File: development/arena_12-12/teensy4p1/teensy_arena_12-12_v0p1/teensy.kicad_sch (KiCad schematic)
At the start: 41 parts, among them J2 Conn_01x04, J3 Conn_01x04, U1 Teensy4.1, U2 74LVC2G17

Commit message: Finished preliminary layout for new 12-12 teensy 4.1 arena.
Includes source termination resistors and schmitt trigger buffers.
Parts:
- C1: footprint Capacitor_SMD:C_0603_1608Metric -> Capacitor_SMD:C_0402_1005Metric
- R10, R11, R12, R13, R14, R15, R16, R17, R18, R19, R20, R21, R22, R23, R24, R25, R26, R27, R28, R29, R3, R30, R31, R32, R33, R34, R35, R36, R37, R38, R4, R5, R6, R7, R8, R9: footprint Resistor_SMD:R_0603_1608Metric -> Resistor_SMD:R_0402_1005Metric
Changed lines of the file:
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@@
 			)
 		)
-		(property "Footprint" "Resistor_SMD:R_0603_1608Metric"
+		(property "Footprint" "Resistor_SMD:R_0402_1005Metric"
 			(at 255.27 147.828 90)
 			(effects
@@
 			)
 		)
-		(property "Footprint" "Resistor_SMD:R_0603_1608Metric"
+		(property "Footprint" "Resistor_SMD:R_0402_1005Metric"
 			(at 255.27 183.388 90)
 			(effects
@@
 			)
 		)
-		(property "Footprint" "Resistor_SMD:R_0603_1608Metric"
+		(property "Footprint" "Resistor_SMD:R_0402_1005Metric"
 			(at 255.27 112.268 90)
 			(effects
@@
 			)
 		)
-		(property "Footprint" "Resistor_SMD:R_0603_1608Metric"
+		(property "Footprint" "Resistor_SMD:R_0402_1005Metric"
 			(at 255.27 42.418 90)
 			(effects
@@
 			)
 		)
-		(property "Footprint" "Resistor_SMD:R_0603_1608Metric"
+		(property "Footprint" "Resistor_SMD:R_0402_1005Metric"
 			(at 255.27 61.468 90)
 			(effects
@@
 			)
 		)
-		(property "Footprint" "Resistor_SMD:R_0603_1608Metric"
+		(property "Footprint" "Resistor_SMD:R_0402_1005Metric"
 			(at 255.27 218.948 90)
 			(effects
@@
 			)
 		)
-		(property "Footprint" "Resistor_SMD:R_0603_1608Metric"
+		(property "Footprint" "Resistor_SMD:R_0402_1005Metric"
 			(at 255.27 122.428 90)
 			(effects
@@
 			)
 		)
-		(property "Footprint" "Resistor_SMD:R_0603_1608Metric"
+		(property "Footprint" "Resistor_SMD:R_0402_1005Metric"
 			(at 255.27 28.448 90)
 			(effects
@@
 			)
 		)
-		(property "Footprint" "Resistor_SMD:R_0603_1608Metric"
+		(property "Footprint" "Resistor_SMD:R_0402_1005Metric"
 			(at 255.27 132.588 90)
 			(effects
@@
 			)
 		)
-		(property "Footprint" "Resistor_SMD:R_0603_1608Metric"
+		(property "Footprint" "Resistor_SMD:R_0402_1005Metric"
 			(at 255.27 168.148 90)
 			(effects
@@
 			)
 		)
-		(property "Footprint" "Resistor_SMD:R_0603_1608Metric"
+		(property "Footprint" "Resistor_SMD:R_0402_1005Metric"
 			(at 255.27 33.528 90)
 			(effects
@@
 			)
 		)
-		(property "Footprint" "Resistor_SMD:R_0603_1608Metric"
+		(property "Footprint" "Resistor_SMD:R_0402_1005Metric"
 			(at 255.27 157.988 90)
 			(effects
@@
 			)
 		)
-		(property "Footprint" "Capacitor_SMD:C_0603_1608Metric"
+		(property "Footprint" "Capacitor_SMD:C_0402_1005Metric"
 			(at 155.9052 199.39 0)
 			(effects
@@
 			)
 		)
-		(property "Footprint" "Resistor_SMD:R_0603_1608Metric"
+		(property "Footprint" "Resistor_SMD:R_0402_1005Metric"
 			(at 255.27 76.708 90)
 			(effects
@@
 			)
 		)
-		(property "Footprint" "Resistor_SMD:R_0603_1608Metric"
+		(property "Footprint" "Resistor_SMD:R_0402_1005Metric"
 			(at 255.27 173.228 90)
 			(effects
@@
 			)
 		)
-		(property "Footprint" "Resistor_SMD:R_0603_1608Metric"
+		(property "Footprint" "Resistor_SMD:R_0402_1005Metric"
 			(at 255.27 91.948 90)
 			(effects
@@
 			)
 		)
-		(property "Footprint" "Resistor_SMD:R_0603_1608Metric"
+		(property "Footprint" "Resistor_SMD:R_0402_1005Metric"
 			(at 255.27 142.748 90)
 			(effects
@@
 			)
 		)
-		(property "Footprint" "Resistor_SMD:R_0603_1608Metric"
+		(property "Footprint" "Resistor_SMD:R_0402_1005Metric"
 			(at 255.27 198.628 90)
 			(effects
@@
 			)
 		)
-		(property "Footprint" "Resistor_SMD:R_0603_1608Metric"
+		(property "Footprint" "Resistor_SMD:R_0402_1005Metric"
 			(at 255.27 188.468 90)
 			(effects
@@
 			)
 		)
-		(property "Footprint" "Resistor_SMD:R_0603_1608Metric"
+		(property "Footprint" "Resistor_SMD:R_0402_1005Metric"
 			(at 255.27 81.788 90)
 			(effects
@@
 			)
 		)
-		(property "Footprint" "Resistor_SMD:R_0603_1608Metric"
+		(property "Footprint" "Resistor_SMD:R_0402_1005Metric"
 			(at 255.27 47.498 90)
 			(effects
@@
 			)
 		)
-		(property "Footprint" "Resistor_SMD:R_0603_1608Metric"
+		(property "Footprint" "Resistor_SMD:R_0402_1005Metric"
 			(at 255.27 163.068 90)
 			(effects
@@
 			)
 		)
-		(property "Footprint" "Resistor_SMD:R_0603_1608Metric"
+		(property "Footprint" "Resistor_SMD:R_0402_1005Metric"
 			(at 255.27 213.868 90)
 			(effects
@@
 			)
 		)
-		(property "Footprint" "Resistor_SMD:R_0603_1608Metric"
+		(property "Footprint" "Resistor_SMD:R_0402_1005Metric"
 			(at 255.27 71.628 90)
 			(effects
@@
 			)
 		)
-		(property "Footprint" "Resistor_SMD:R_0603_1608Metric"
+		(property "Footprint" "Resistor_SMD:R_0402_1005Metric"
 			(at 255.27 193.548 90)
 			(effects
@@
 			)
 		)
-		(property "Footprint" "Resistor_SMD:R_0603_1608Metric"
+		(property "Footprint" "Resistor_SMD:R_0402_1005Metric"
 			(at 255.27 107.188 90)
 			(effects
@@
 			)
 		)
-		(property "Footprint" "Resistor_SMD:R_0603_1608Metric"
+		(property "Footprint" "Resistor_SMD:R_0402_1005Metric"
 			(at 255.27 178.308 90)
 			(effects
@@
 			)
 		)
-		(property "Footprint" "Resistor_SMD:R_0603_1608Metric"
+		(property "Footprint" "Resistor_SMD:R_0402_1005Metric"
 			(at 255.27 56.388 90)
 			(effects
@@
 			)
 		)
-		(property "Footprint" "Resistor_SMD:R_0603_1608Metric"
+		(property "Footprint" "Resistor_SMD:R_0402_1005Metric"
 			(at 255.27 203.708 90)
 			(effects
@@
 			)
 		)
-		(property "Footprint" "Resistor_SMD:R_0603_1608Metric"
+		(property "Footprint" "Resistor_SMD:R_0402_1005Metric"
 			(at 255.27 127.508 90)
 			(effects
@@
 			)
 		)
-		(property "Footprint" "Resistor_SMD:R_0603_1608Metric"
+		(property "Footprint" "Resistor_SMD:R_0402_1005Metric"
 			(at 255.27 117.348 90)
 			(effects
@@
 			)
 		)
-		(property "Footprint" "Resistor_SMD:R_0603_1608Metric"
+		(property "Footprint" "Resistor_SMD:R_0402_1005Metric"
 			(at 255.27 97.028 90)
 			(effects
@@
 			)
 		)
-		(property "Footprint" "Resistor_SMD:R_0603_1608Metric"
+		(property "Footprint" "Resistor_SMD:R_0402_1005Metric"
 			(at 255.27 102.108 90)
 			(effects
@@
 			)
 		)
-		(property "Footprint" "Resistor_SMD:R_0603_1608Metric"
+		(property "Footprint" "Resistor_SMD:R_0402_1005Metric"
 			(at 255.27 86.868 90)
 			(effects
@@
 			)
 		)
-		(property "Footprint" "Resistor_SMD:R_0603_1608Metric"
+		(property "Footprint" "Resistor_SMD:R_0402_1005Metric"
 			(at 255.27 66.548 90)
 			(effects
@@
 			)
 		)
-		(property "Footprint" "Resistor_SMD:R_0603_1608Metric"
+		(property "Footprint" "Resistor_SMD:R_0402_1005Metric"
 			(at 255.27 137.668 90)
 			(effects
@@
 			)
 		)
-		(property "Footprint" "Resistor_SMD:R_0603_1608Metric"
+		(property "Footprint" "Resistor_SMD:R_0402_1005Metric"
 			(at 255.27 152.908 90)
 			(effects

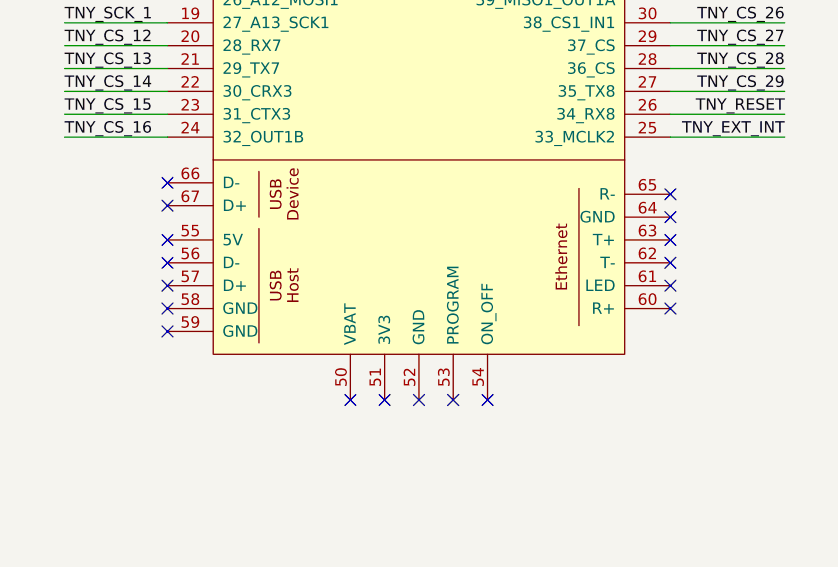
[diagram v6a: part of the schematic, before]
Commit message: Worked on prelimnary hand routing of 12-12 teensy 4.1 arena.
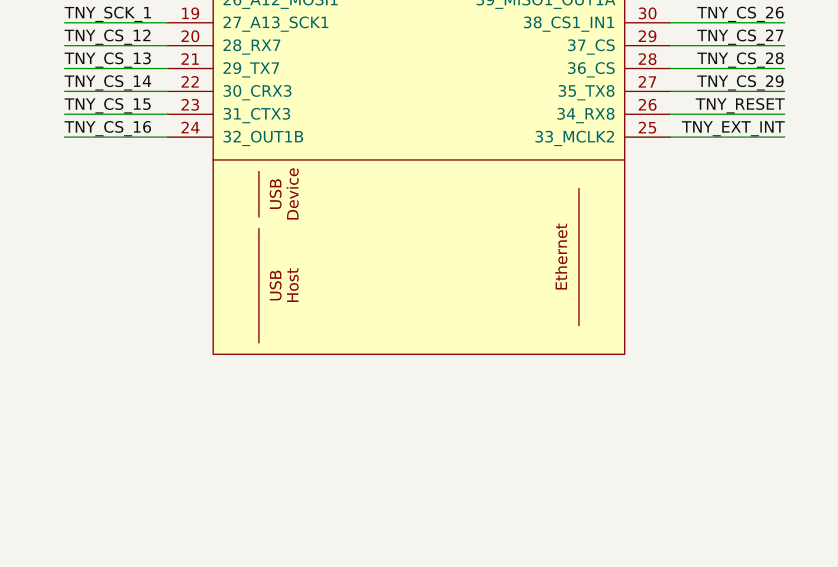
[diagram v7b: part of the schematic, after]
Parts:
- U1: footprint teensy:Teensy41 -> teensy:Teensy41_outer_only
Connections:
- no-connect marks 20 -> 2
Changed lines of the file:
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@@
 	)
 	(no_connect
-		(at 130.81 106.68)
-	)
-	(no_connect
-		(at 110.49 119.38)
-	)
-	(no_connect
-		(at 74.93 95.25)
-	)
-	(no_connect
-		(at 74.93 97.79)
-	)
-	(no_connect
 		(at 130.81 31.75)
 	)
 	(no_connect
-		(at 130.81 104.14)
-	)
-	(no_connect
-		(at 74.93 106.68)
-	)
-	(no_connect
-		(at 74.93 109.22)
-	)
-	(no_connect
-		(at 106.68 119.38)
-	)
-	(no_connect
-		(at 130.81 99.06)
-	)
-	(no_connect
-		(at 130.81 109.22)
-	)
-	(no_connect
 		(at 130.81 27.94)
 	)
-	(no_connect
-		(at 99.06 119.38)
-	)
-	(no_connect
-		(at 74.93 104.14)
-	)
-	(no_connect
-		(at 102.87 119.38)
-	)
-	(no_connect
-		(at 95.25 119.38)
-	)
-	(no_connect
-		(at 130.81 96.52)
-	)
-	(no_connect
-		(at 74.93 101.6)
-	)
-	(no_connect
-		(at 130.81 101.6)
-	)
-	(no_connect
-		(at 74.93 111.76)
-	)
 	(bus_entry
 		(at 326.39 72.39)
@@
 			)
 		)
-		(property "Footprint" "teensy:Teensy41"
+		(property "Footprint" "teensy:Teensy41_outer_only"
 			(at 92.71 76.2 0)
 			(effects
@@
 		(pin "5"
 		)
-		(pin "50"
-		)
-		(pin "51"
-		)
-		(pin "53"
-		)
-		(pin "54"
-		)
-		(pin "55"
-		)
-		(pin "56"
-		)
-		(pin "57"
-		)
-		(pin "58"
-		)
-		(pin "59"
-		)
 		(pin "6"
 		)
-		(pin "60"
-		)
-		(pin "61"
-		)
-		(pin "62"
-		)
-		(pin "63"
-		)
-		(pin "64"
-		)
-		(pin "65"
-		)
-		(pin "66"
-		)
-		(pin "67"
-		)
 		(pin "7"
 		)
@@
 		(pin "47"
 		)
-		(pin "52"
-		)
 		(pin "1"

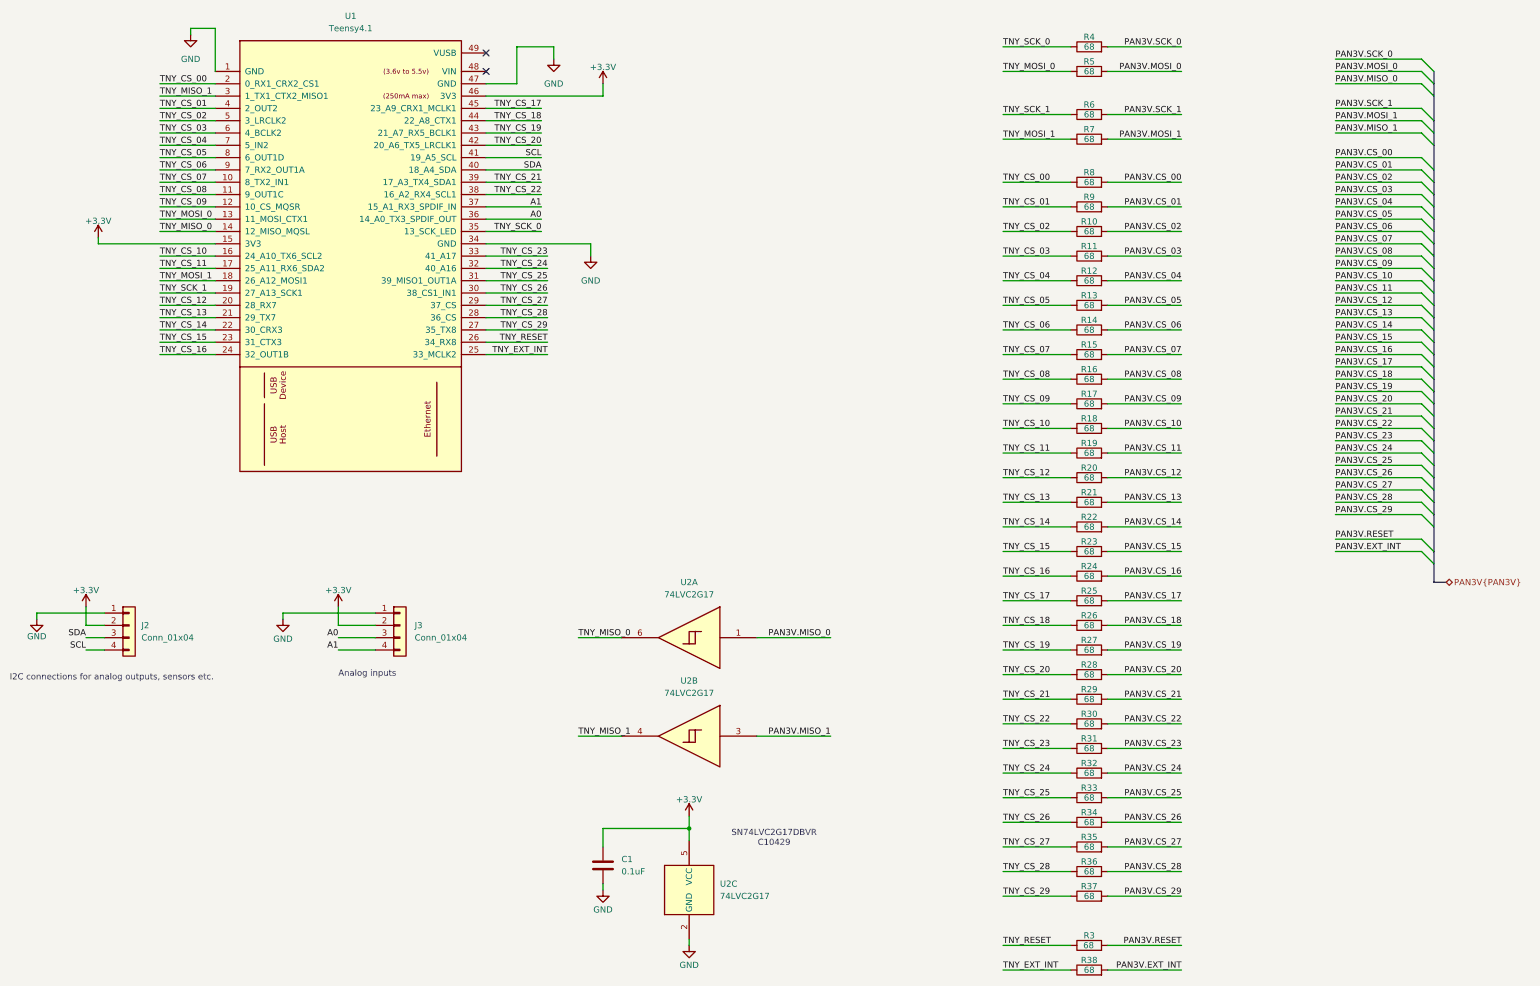
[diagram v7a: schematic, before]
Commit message: Finished initial verions of fab files for 12-12 teensy 4.1 arena. Need to check orientations.
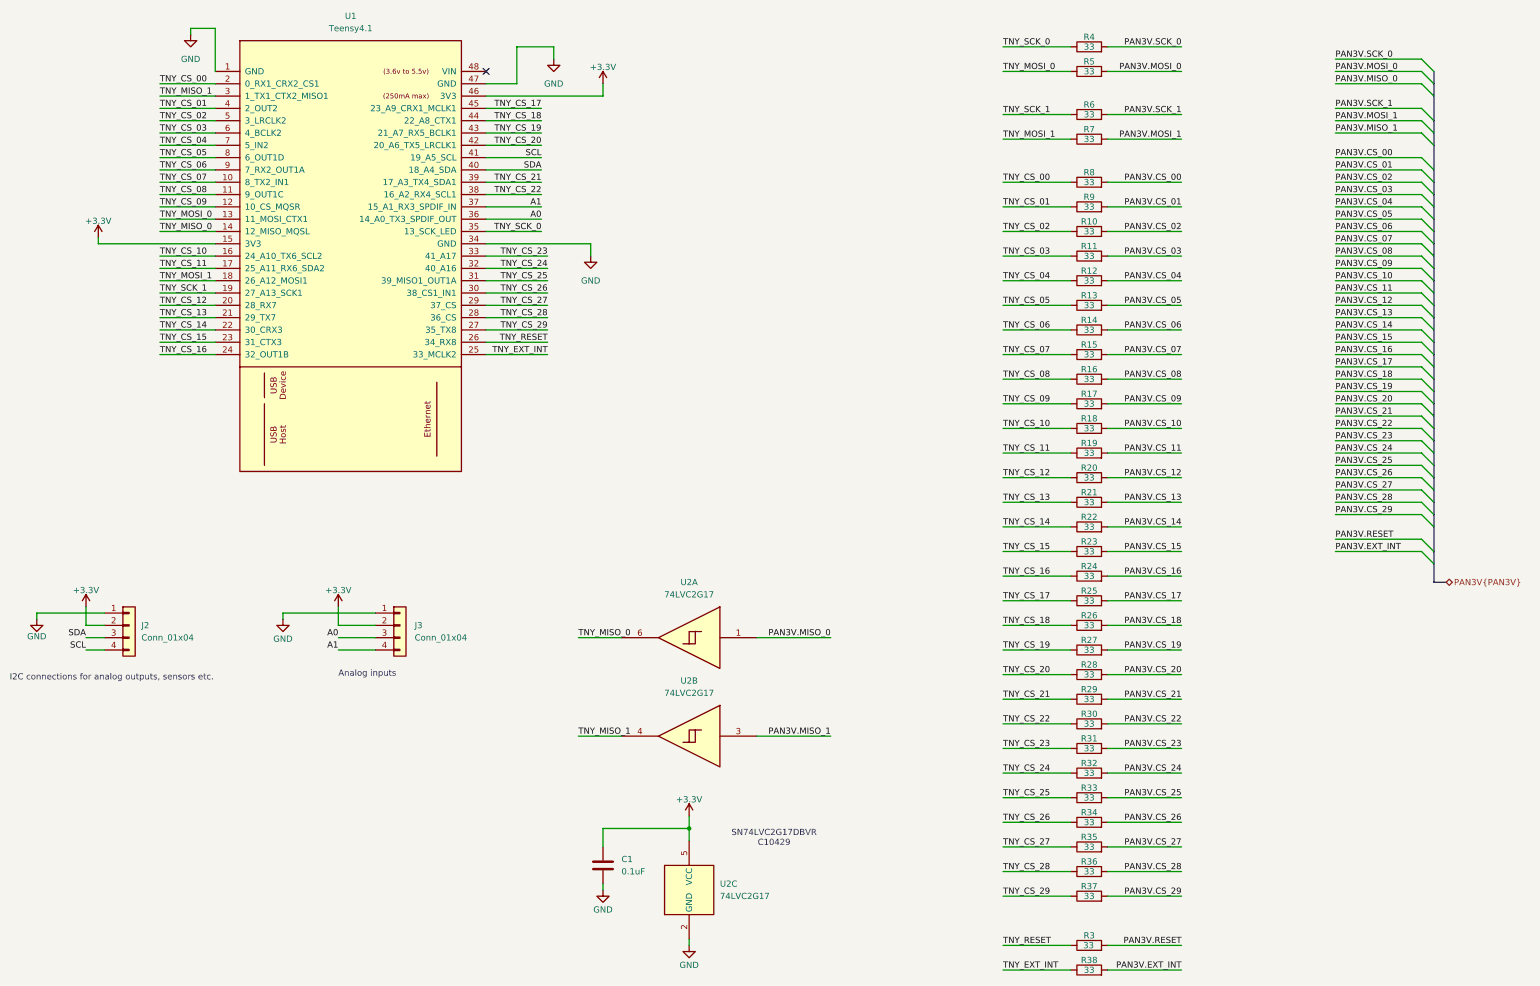
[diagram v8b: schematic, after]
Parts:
- R10, R11, R12, R13, R14, R15, R16, R17, R18, R19, R20, R21, R22, R23, R24, R25, R26, R27, R28, R29, R3, R30, R31, R32, R33, R34, R35, R36, R37, R38, R4, R5, R6, R7, R8, R9: value 68 -> 33
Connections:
- no-connect marks 2 -> 1
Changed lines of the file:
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@@
 		(at 130.81 31.75)
 	)
-	(no_connect
-		(at 130.81 27.94)
-	)
 	(bus_entry
 		(at 326.39 72.39)
@@
 			)
 		)
-		(property "Value" "68"
+		(property "Value" "33"
 			(at 255.27 146.05 90)
 			(effects
@@
 			)
 		)
-		(property "Value" "68"
+		(property "Value" "33"
 			(at 255.27 181.61 90)
 			(effects
@@
 			)
 		)
-		(property "Value" "68"
+		(property "Value" "33"
 			(at 255.27 110.49 90)
 			(effects
@@
 			)
 		)
-		(property "Value" "68"
+		(property "Value" "33"
 			(at 255.27 40.64 90)
 			(effects
@@
 			)
 		)
-		(property "Value" "68"
+		(property "Value" "33"
 			(at 255.27 59.69 90)
 			(effects
@@
 			)
 		)
-		(property "Value" "68"
+		(property "Value" "33"
 			(at 255.27 217.17 90)
 			(effects
@@
 			)
 		)
-		(property "Value" "68"
+		(property "Value" "33"
 			(at 255.27 120.65 90)
 			(effects
@@
 			)
 		)
-		(property "Value" "68"
+		(property "Value" "33"
 			(at 255.27 26.67 90)
 			(effects
@@
 		(pin "48"
 		)
-		(pin "49"
-		)
 		(pin "5"
 		)
@@
 			)
 		)
-		(property "Value" "68"
+		(property "Value" "33"
 			(at 255.27 130.81 90)
 			(effects
@@
 			)
 		)
-		(property "Value" "68"
+		(property "Value" "33"
 			(at 255.27 166.37 90)
 			(effects
@@
 			)
 		)
-		(property "Value" "68"
+		(property "Value" "33"
 			(at 255.27 31.75 90)
 			(effects
@@
 			)
 		)
-		(property "Value" "68"
+		(property "Value" "33"
 			(at 255.27 156.21 90)
 			(effects
@@
 			)
 		)
-		(property "Value" "68"
+		(property "Value" "33"
 			(at 255.27 74.93 90)
 			(effects
@@
 			)
 		)
-		(property "Value" "68"
+		(property "Value" "33"
 			(at 255.27 171.45 90)
 			(effects
@@
 			)
 		)
-		(property "Value" "68"
+		(property "Value" "33"
 			(at 255.27 90.17 90)
 			(effects
@@
 			)
 		)
-		(property "Value" "68"
+		(property "Value" "33"
 			(at 255.27 140.97 90)
 			(effects
@@
 			)
 		)
-		(property "Value" "68"
+		(property "Value" "33"
 			(at 255.27 196.85 90)
 			(effects
@@
 			)
 		)
-		(property "Value" "68"
+		(property "Value" "33"
 			(at 255.27 186.69 90)
 			(effects
@@
 			)
 		)
-		(property "Value" "68"
+		(property "Value" "33"
 			(at 255.27 80.01 90)
 			(effects
@@
 			)
 		)
-		(property "Value" "68"
+		(property "Value" "33"
 			(at 255.27 45.72 90)
 			(effects
@@
 			)
 		)
-		(property "Value" "68"
+		(property "Value" "33"
 			(at 255.27 161.29 90)
 			(effects
@@
 			)
 		)
-		(property "Value" "68"
+		(property "Value" "33"
 			(at 255.143 212.09 90)
 			(effects
@@
 			)
 		)
-		(property "Value" "68"
+		(property "Value" "33"
 			(at 255.27 69.85 90)
 			(effects
@@
 			)
 		)
-		(property "Value" "68"
+		(property "Value" "33"
 			(at 255.27 191.77 90)
 			(effects
@@
 			)
 		)
-		(property "Value" "68"
+		(property "Value" "33"
 			(at 255.27 105.41 90)
 			(effects
@@
 			)
 		)
-		(property "Value" "68"
+		(property "Value" "33"
 			(at 255.27 176.53 90)
 			(effects
@@
 			)
 		)
-		(property "Value" "68"
+		(property "Value" "33"
 			(at 255.27 54.61 90)
 			(effects
@@
 			)
 		)
-		(property "Value" "68"
+		(property "Value" "33"
 			(at 255.27 201.93 90)
 			(effects
@@
 			)
 		)
-		(property "Value" "68"
+		(property "Value" "33"
 			(at 255.27 125.73 90)
 			(effects
@@
 			)
 		)
-		(property "Value" "68"
+		(property "Value" "33"
 			(at 255.27 115.57 90)
 			(effects
@@
 			)
 		)
-		(property "Value" "68"
+		(property "Value" "33"
 			(at 255.27 95.25 90)
 			(effects
@@
 			)
 		)
-		(property "Value" "68"
+		(property "Value" "33"
 			(at 255.27 100.33 90)
 			(effects
@@
 			)
 		)
-		(property "Value" "68"
+		(property "Value" "33"
 			(at 255.27 85.09 90)
 			(effects
@@
 			)
 		)
-		(property "Value" "68"
+		(property "Value" "33"
 			(at 255.27 64.77 90)
 			(effects
@@
 			)
 		)
-		(property "Value" "68"
+		(property "Value" "33"
 			(at 255.27 135.89 90)
 			(effects
@@
 			)
 		)
-		(property "Value" "68"
+		(property "Value" "33"
 			(at 255.27 151.13 90)
 			(effects
